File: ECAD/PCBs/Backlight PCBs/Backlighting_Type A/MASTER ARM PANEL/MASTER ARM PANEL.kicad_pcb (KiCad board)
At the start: 2 copper layers, 45.7 x 123.5 mm, 43 parts, among them J1 BL IN, J2 BL OUT, J3 READY, J4 MASTER MODE, SW1 READY, SW2 A/A, SW3 A/G

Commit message: Drawing Sheet & Silkscreen update - Backlight Panels (Fc thru Spin)
1:  Updated/Relinked Drawing Sheet for both PCB and Schematics
2:  Standardized Silkscreen (if required)

Finished Remaining Backlighting Type A & Type B PCBs.....
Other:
- board text added: "MASTER ARM PANEL Revision: 3 www.openhornet.com"
- board text removed: "MASTER ARM Panel Backlight Designed by L. Walker"
- board text removed: "Version 2.3"
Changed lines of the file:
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@@
   )
   (paper "A4")
+  (title_block
+    (title "MASTER ARM PANEL")
+    (date "2023-02-10")
+    (rev "3")
+  )
   (layers
     (0 "F.Cu" mixed)
@@
     (effects (font (size 1 1) (thickness 0.15)) (justify mirror))
   )
-  (gr_text "Version 2.3" (at 219.16848 60.51948) (layer "B.SilkS")
-    (effects (font (size 1 1) (thickness 0.15)) (justify mirror))
-  )
   (gr_text "GND" (at 226.36938 94.55548) (layer "B.SilkS")
     (effects (font (size 1 1) (thickness 0.15)) (justify mirror))
@@
     (effects (font (size 1 1) (thickness 0.15)) (justify mirror))
   )
-  (gr_text "MASTER ARM Panel Backlight\nDesigned by L. Walker" (at 239.92488 117.69958) (layer "B.SilkS")
-    (effects (font (size 1 1) (thickness 0.15)) (justify left mirror))
+  (gr_text "MASTER ARM PANEL\nRevision: 3\nwww.openhornet.com" (at 223.42298 119.05378) (layer "B.SilkS")
+    (effects (font (size 1 1) (thickness 0.15)) (justify mirror))
   )
   (gr_text "THRU" (at 199.20408 96.25728 270) (layer "B.SilkS")

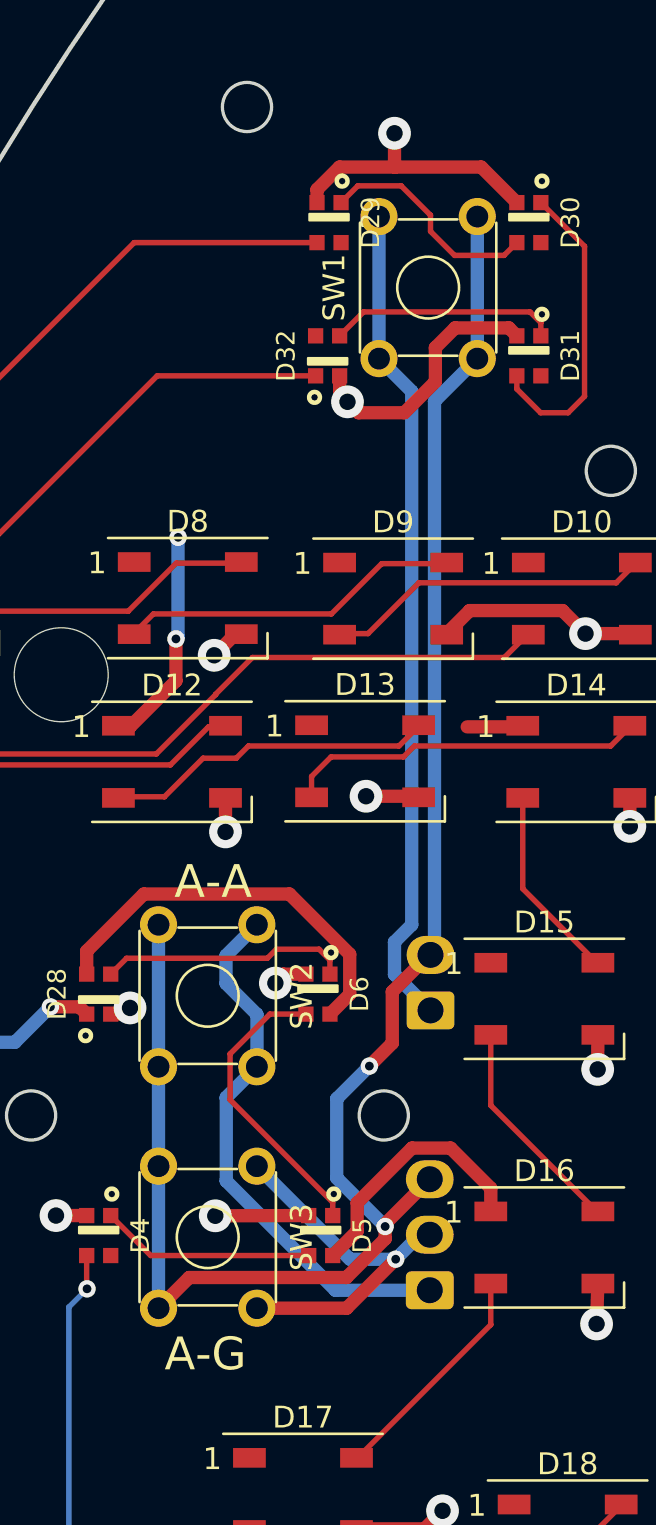
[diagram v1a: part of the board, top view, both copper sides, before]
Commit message: Review: LEFT CB thru OBOGS 100%
Reviewed/adjusted silkscreens as needed
Relinked footprints
Updated Manufacturing files
Updated PNGs and STEP files as needed.
Renamed PNGs for standardization
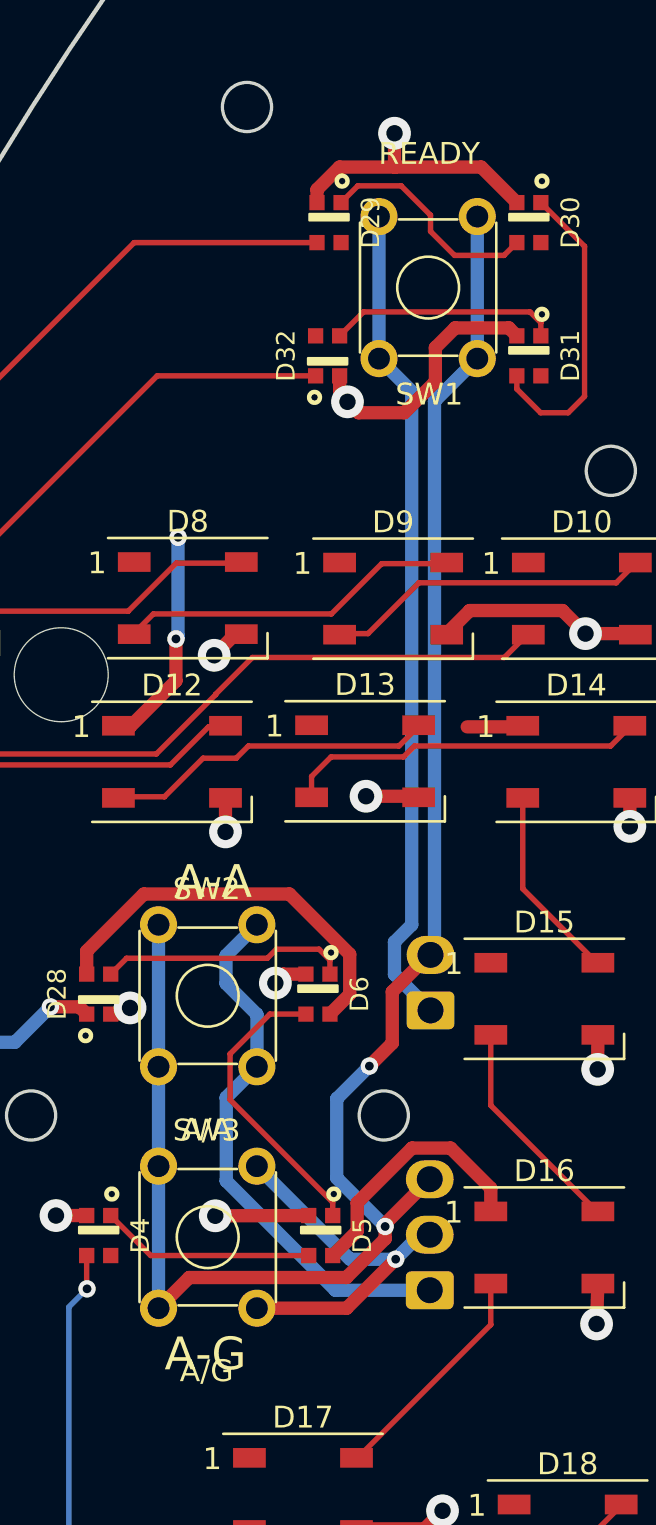
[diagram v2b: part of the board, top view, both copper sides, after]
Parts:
- SW1, SW2, SW3: footprint Button_Switch_THT:SW_TH_Tactile_Omron_B3F-10xx -> OH_Footprints:SW_TH_Tactile_Omron_B3F-10xx
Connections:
- SW1 pad 3: GND -> (no net)
- SW1 pad 4: GND -> (no net)
- SW2 pad 3: GND -> (no net)
- SW2 pad 4: GND -> (no net)
- SW3 pad 3: GND -> (no net)
- SW3 pad 4: GND -> (no net)

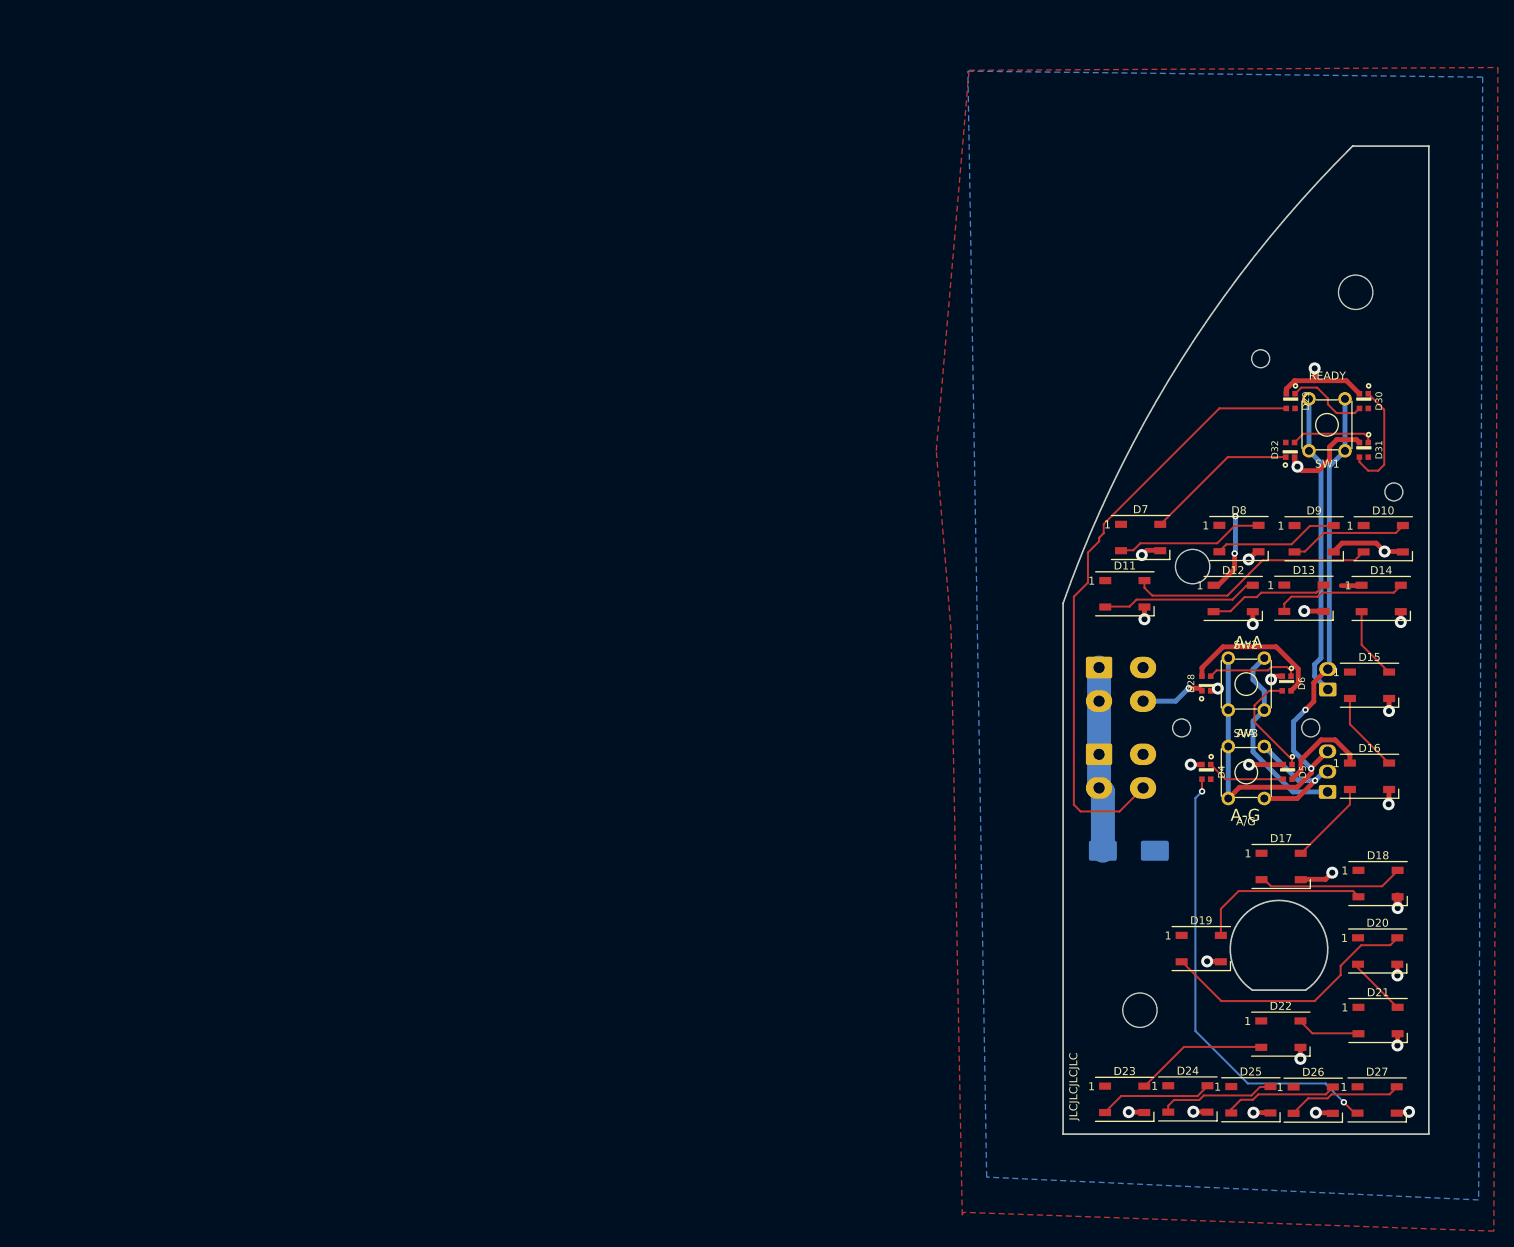
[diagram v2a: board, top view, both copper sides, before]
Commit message: KiCad 7 Transition - MASTER ARM Panel
Rotated WS2812B-2020 LEDs (x8) to fix misrouting.  Issue #897

PCB and Schematic standardization
Updated silkscreen text
Adjusted traces to prevent conflicts
Add Testpoints
Recompiled assets and manufacturing files
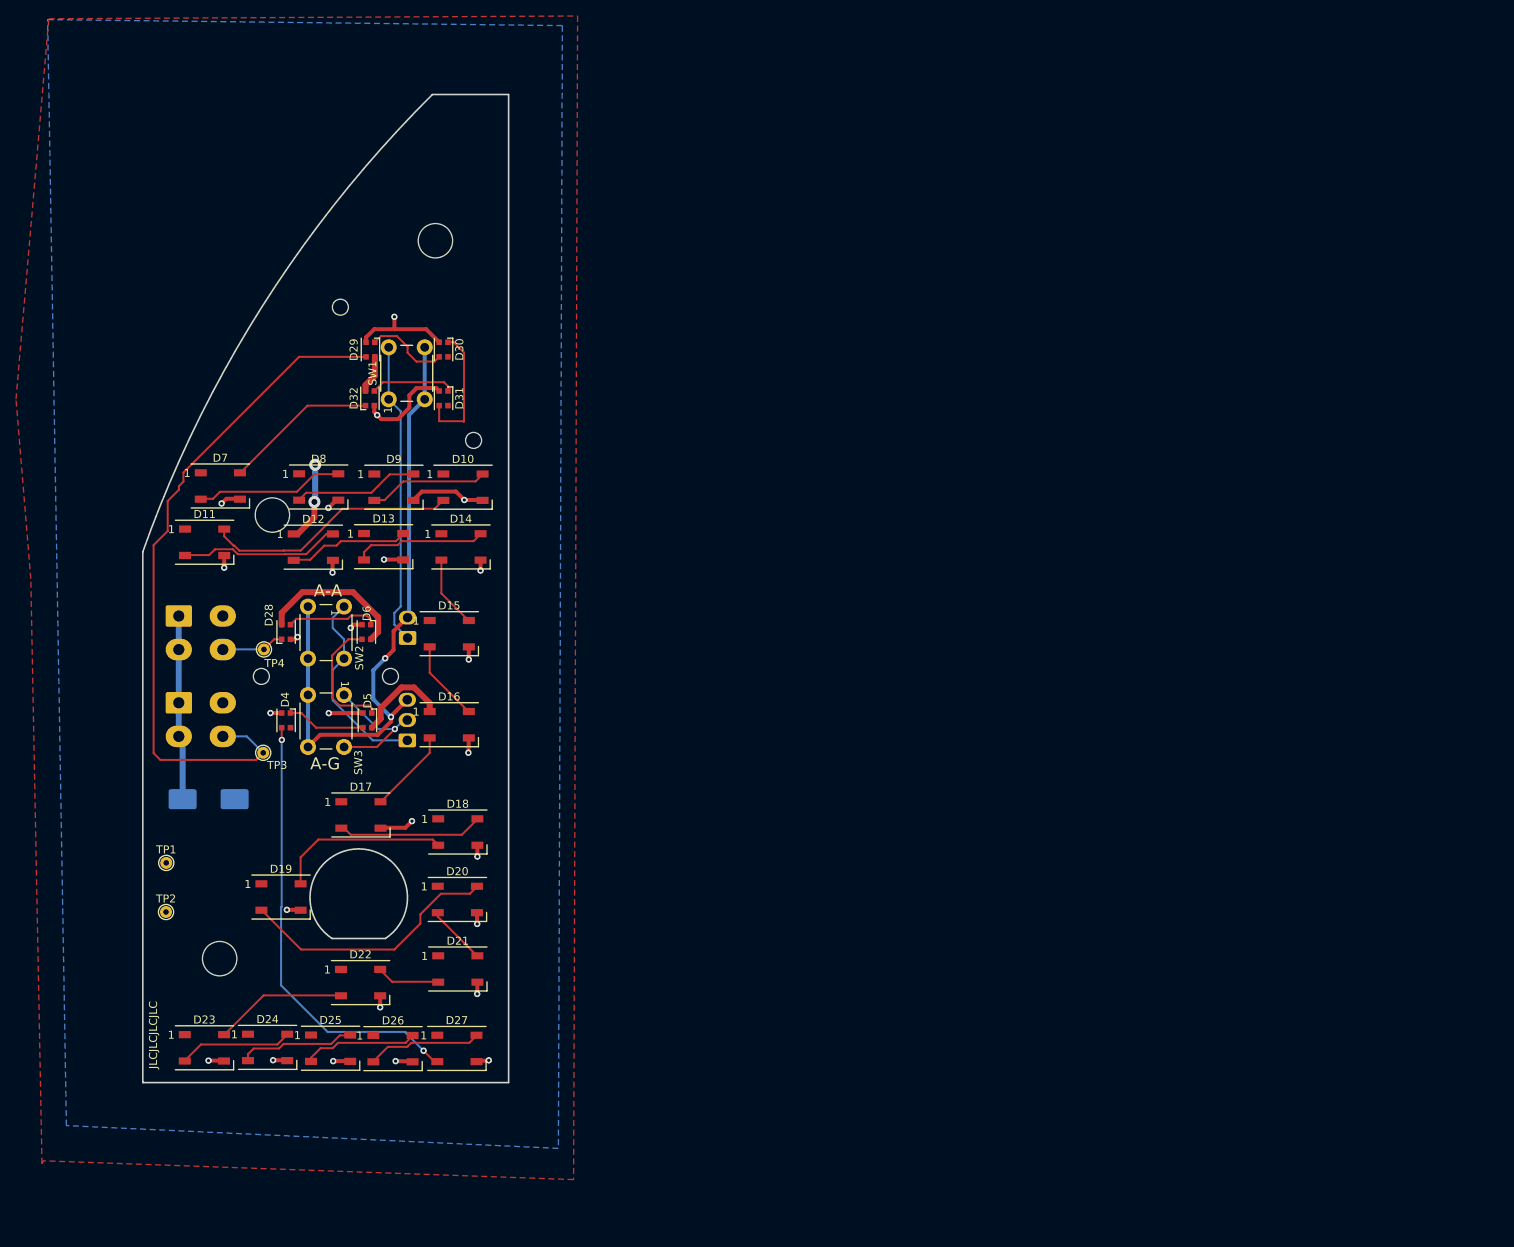
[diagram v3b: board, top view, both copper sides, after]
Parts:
- added MH4: #0-80/2mm, OH_Footprints:MountingHole_#0-80_2mm, B.Cu at (108.0, 49.2)
- added MH5: #0-80/2mm, OH_Footprints:MountingHole_#0-80_2mm, B.Cu at (124.6, 65.9)
- added MH6: #0-80/2mm, OH_Footprints:MountingHole_#0-80_2mm, B.Cu at (98.1, 95.4)
- added MH7: #0-80/2mm, OH_Footprints:MountingHole_#0-80_2mm, B.Cu at (114.2, 95.4)
- added TP1: TestPoint, OH_Footprints:TestPoint_THTPad_D1.5mm_Drill0.7mm, F.Cu at (86.2, 118.7)
- added TP2: TestPoint, OH_Footprints:TestPoint_THTPad_D1.5mm_Drill0.7mm, F.Cu at (86.2, 124.8)
- added TP3: TestPoint, OH_Footprints:TestPoint_THTPad_D1.5mm_Drill0.7mm, F.Cu at (98.3, 104.9)
- added TP4: TestPoint, OH_Footprints:TestPoint_THTPad_D1.5mm_Drill0.7mm, F.Cu at (98.4, 92.0)
- C1: value C_Polarized -> 1000uF
- D10, D11, D12, D13, D14, D15, D16, D17, D18, D19, D20, D21, D22, D23, D24, D25, D26, D27, D7, D8, D9: footprint OH_Footprints:LED_WS2812B_PLCC4_5.0x5.0mm_P3.2mm -> LED_SMD:LED_WS2812B_PLCC4_5.0x5.0mm_P3.2mm
- D28, D29, D30, D31, D32, D4, D5, D6: footprint OH_Footprints:WS2812-2020 -> OH_Footprints:LED_WS2812B-2020_PLCC4_2.0x2.0mm
- J1: value BL IN -> Mini-Fit Jr. 2x02
- J2: value BL OUT -> Mini-Fit Jr. 2x02
- J3: value READY -> KK-254 1x02
- J4: value MASTER MODE -> KK-254 1x03
- LOGO1: renamed from LOGO2; value OpenHornetLogoSmall -> LOGO; footprint OH_Footprints:OH_LOGO_37.7mm_5.9mm -> OH_Footprints:LOGO_OH_Text_Small
- LOGO2: renamed from LOGO1; value CC-BY-NC-SA_Icon -> LOGO; footprint OH_Footprints:CC-BY-NC-SA-Small -> OH_Footprints:LOGO_CC-BY-NC-SA_Half_Small
- LOGO3: value OH_S2AL_Silkscreen -> LOGO; moved to B.Cu
- MH1: renamed from H1; value OHPanelScrew -> 6x32 / 4mm; footprint OH_Footprints:OH_Panel_6-32_PHS -> OH_Footprints:MountingHole_6-32_PHS; moved to B.Cu
- MH2: renamed from H2; value OHPanelScrew -> 6x32 / 4mm; footprint OH_Footprints:OH_Panel_6-32_PHS -> OH_Footprints:MountingHole_6-32_PHS; moved to B.Cu
- MH3: renamed from H3; value OHPanelScrew -> 6x32 / 4mm; footprint OH_Footprints:OH_Panel_6-32_PHS -> OH_Footprints:MountingHole_6-32_PHS; moved to B.Cu
- SW1: value READY -> B3F-1026; footprint OH_Footprints:SW_TH_Tactile_Omron_B3F-10xx -> OH_Footprints:Omron_B3F-1026
- SW2: value A/A -> B3F-1026; footprint OH_Footprints:SW_TH_Tactile_Omron_B3F-10xx -> OH_Footprints:Omron_B3F-1026
- SW3: value A/G -> B3F-1026; footprint OH_Footprints:SW_TH_Tactile_Omron_B3F-10xx -> OH_Footprints:Omron_B3F-1026
- moved LOGO2 127.9 mm to (115.6, 142.2)
- moved LOGO1 115.5 mm to (106.6, 138.4)
- moved D14 115.2 mm to (123.0, 79.2)
- moved D15 115.2 mm to (121.6, 90.0)
- moved D16 115.2 mm to (121.6, 101.4)
- moved D19 115.2 mm to (100.5, 122.9)
- moved D20 115.2 mm to (122.6, 123.2)
- moved D28 115.2 mm to (101.2, 89.8), turned to 90 degrees
- moved D29 115.2 mm to (111.7, 54.5), turned to -90 degrees
- moved D30 115.2 mm to (120.9, 54.5), turned to -90 degrees
- moved D31 115.2 mm to (120.9, 60.6), turned to -90 degrees
- moved D32 115.2 mm to (111.7, 60.6), turned to 90 degrees
- moved D4 115.2 mm to (101.2, 100.9), turned to -90 degrees
- moved D5 115.2 mm to (111.3, 100.9), turned to -90 degrees
- moved SW1 115.2 mm to (114.0, 60.7)
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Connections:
- net /DATAIN renamed DATA IN
- net /DATAOUT renamed DATA OUT
- net /LED+5V renamed +5V
- net Net-(D11-Pad2) renamed /DATA1
- net Net-(D20-Pad2) renamed /DATA2
- C1 pad 2: /LEDGND -> GND
- D10 pad 3: /LEDGND -> GND
- D11 pad 3: /LEDGND -> GND
- D12 pad 3: /LEDGND -> GND
- D13 pad 3: /LEDGND -> GND
- D14 pad 3: /LEDGND -> GND
- D15 pad 3: /LEDGND -> GND
- D16 pad 3: /LEDGND -> GND
- D17 pad 3: /LEDGND -> GND
- D18 pad 3: /LEDGND -> GND
- D19 pad 3: /LEDGND -> GND
- D20 pad 3: /LEDGND -> GND
- D21 pad 3: /LEDGND -> GND
- D22 pad 3: /LEDGND -> GND
- D23 pad 3: /LEDGND -> GND
- D24 pad 3: /LEDGND -> GND
- D25 pad 3: /LEDGND -> GND
- D26 pad 3: /LEDGND -> GND
- D27 pad 3: /LEDGND -> GND
- D28 pad 2: /LEDGND -> GND
- D29 pad 2: /LEDGND -> GND
- D30 pad 2: /LEDGND -> GND
- D31 pad 2: /LEDGND -> GND
- D32 pad 2: /LEDGND -> GND
- D4 pad 2: /LEDGND -> GND
- D5 pad 2: /LEDGND -> GND
- D6 pad 2: /LEDGND -> GND
- D7 pad 3: /LEDGND -> GND
- D8 pad 3: /LEDGND -> GND
- D9 pad 3: /LEDGND -> GND
- J1 pad 3: /LEDGND -> GND
- J2 pad 3: /LEDGND -> GND
- SW1 pad 3: (no net) -> GND
- SW1 pad 4: (no net) -> GND
- SW2 pad 3: (no net) -> GND
- SW2 pad 4: (no net) -> GND
- SW3 pad 3: (no net) -> GND
- SW3 pad 4: (no net) -> GND
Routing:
- net /LEDGND: track 79.0 -> 0.00 mm, vias 26 -> 0
- net GND: track 82.7 -> 160.4 mm, vias 2 -> 28
- net DATA IN: track 75.7 -> 85.8 mm
- net Net-(D5-DOUT): track 13.6 -> 16.0 mm
- net +5V: track 66.1 -> 68.3 mm
- net Net-(D30-DOUT): track 14.2 -> 16.2 mm
- net Net-(D27-DOUT): track 56.4 -> 55.4 mm
- net Net-(D10-DOUT): track 30.9 -> 31.6 mm
- net /DATA1: track 19.5 -> 20.0 mm
- net DATA OUT: track 8.17 -> 7.87 mm, vias 1 -> 0
- added copper zone on B.Cu, net GND
- removed copper zone on B.Cu, net /LEDGND
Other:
- outline, holes or cut-outs redrawn
- board text added: "0.2000 mm / 0.0000 mm"
- board text added: "0.3000 mm"
- board text added: "1.6000 mm"
- board text added: "2"
- board text added: "45.7200 mm x 123.5075 mm"
- board text added: "BOARD CHARACTERISTICS"
- board text added: "Board Thickness:"
- board text added: "Board overall dimensions:"
- board text added: "Castellated pads:"
- board text added: "Copper Finish:"
- board text added: "Copper Layer Count:"
- board text added: "Edge card connectors:"
- board text added: "Impedance Control:"
- board text added: "MASTER ARM PANEL REV: 4 WWW.OPENHORNET.COM"
- board text added: "Min hole diameter:"
- board text added: "Min track/spacing:"
- board text added: "No"
- board text added: "None"
- board text added: "Plated Board Edge:"
- board text removed: "IN"
- board text removed: "MASTER ARM PANEL Revision: 3 www.openhornet.com"
- board text removed: "MASTER MODE"
- board text removed: "READY SW"
- board text removed: "THRU"
